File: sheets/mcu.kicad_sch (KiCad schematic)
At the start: 37 parts, among them SW1 SW_Nidec_CAS-120A1, SW2 SW_Push, U1 STM32H755ZIT6, Y1 25M, Y2 Crystal

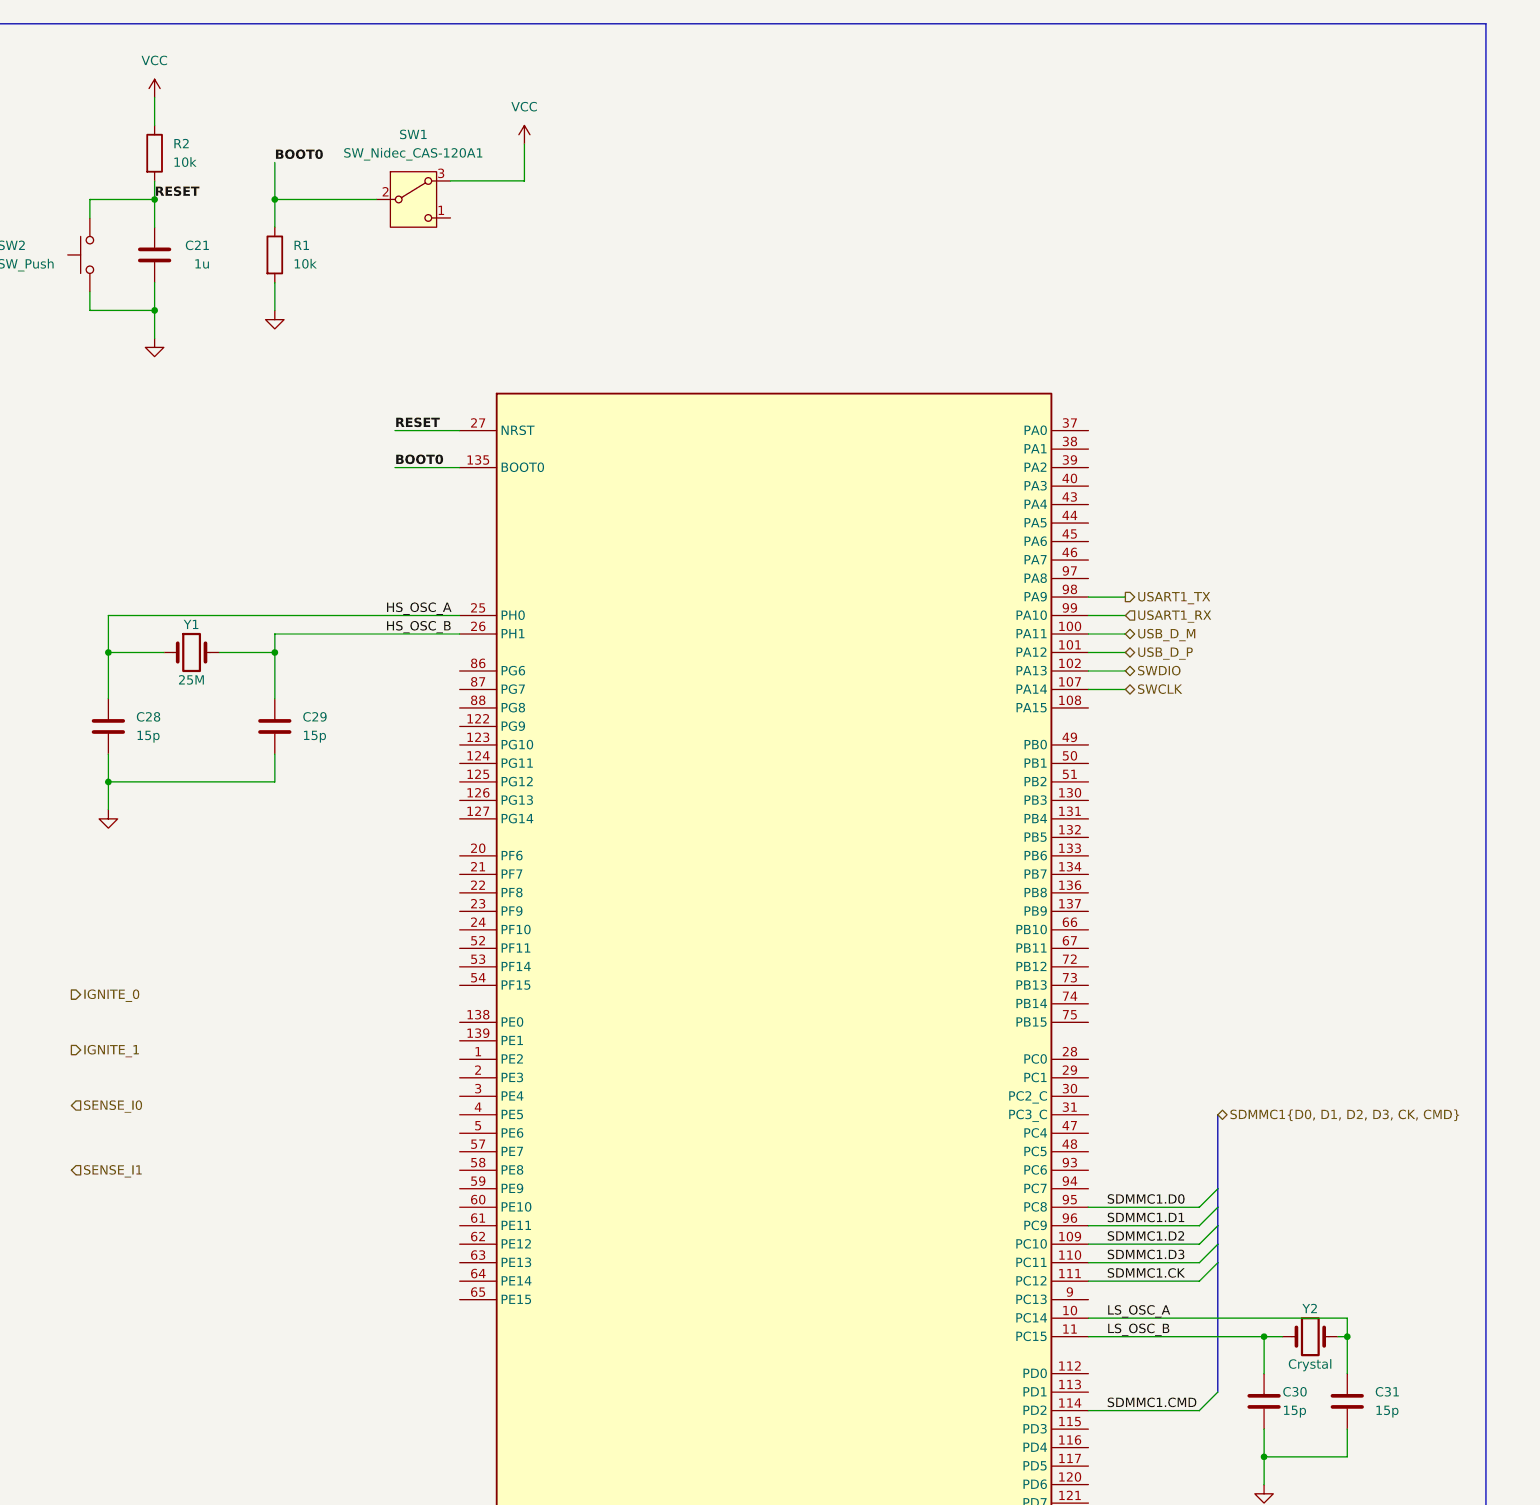
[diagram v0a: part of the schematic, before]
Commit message: added current rush limiting resistors to bmp581
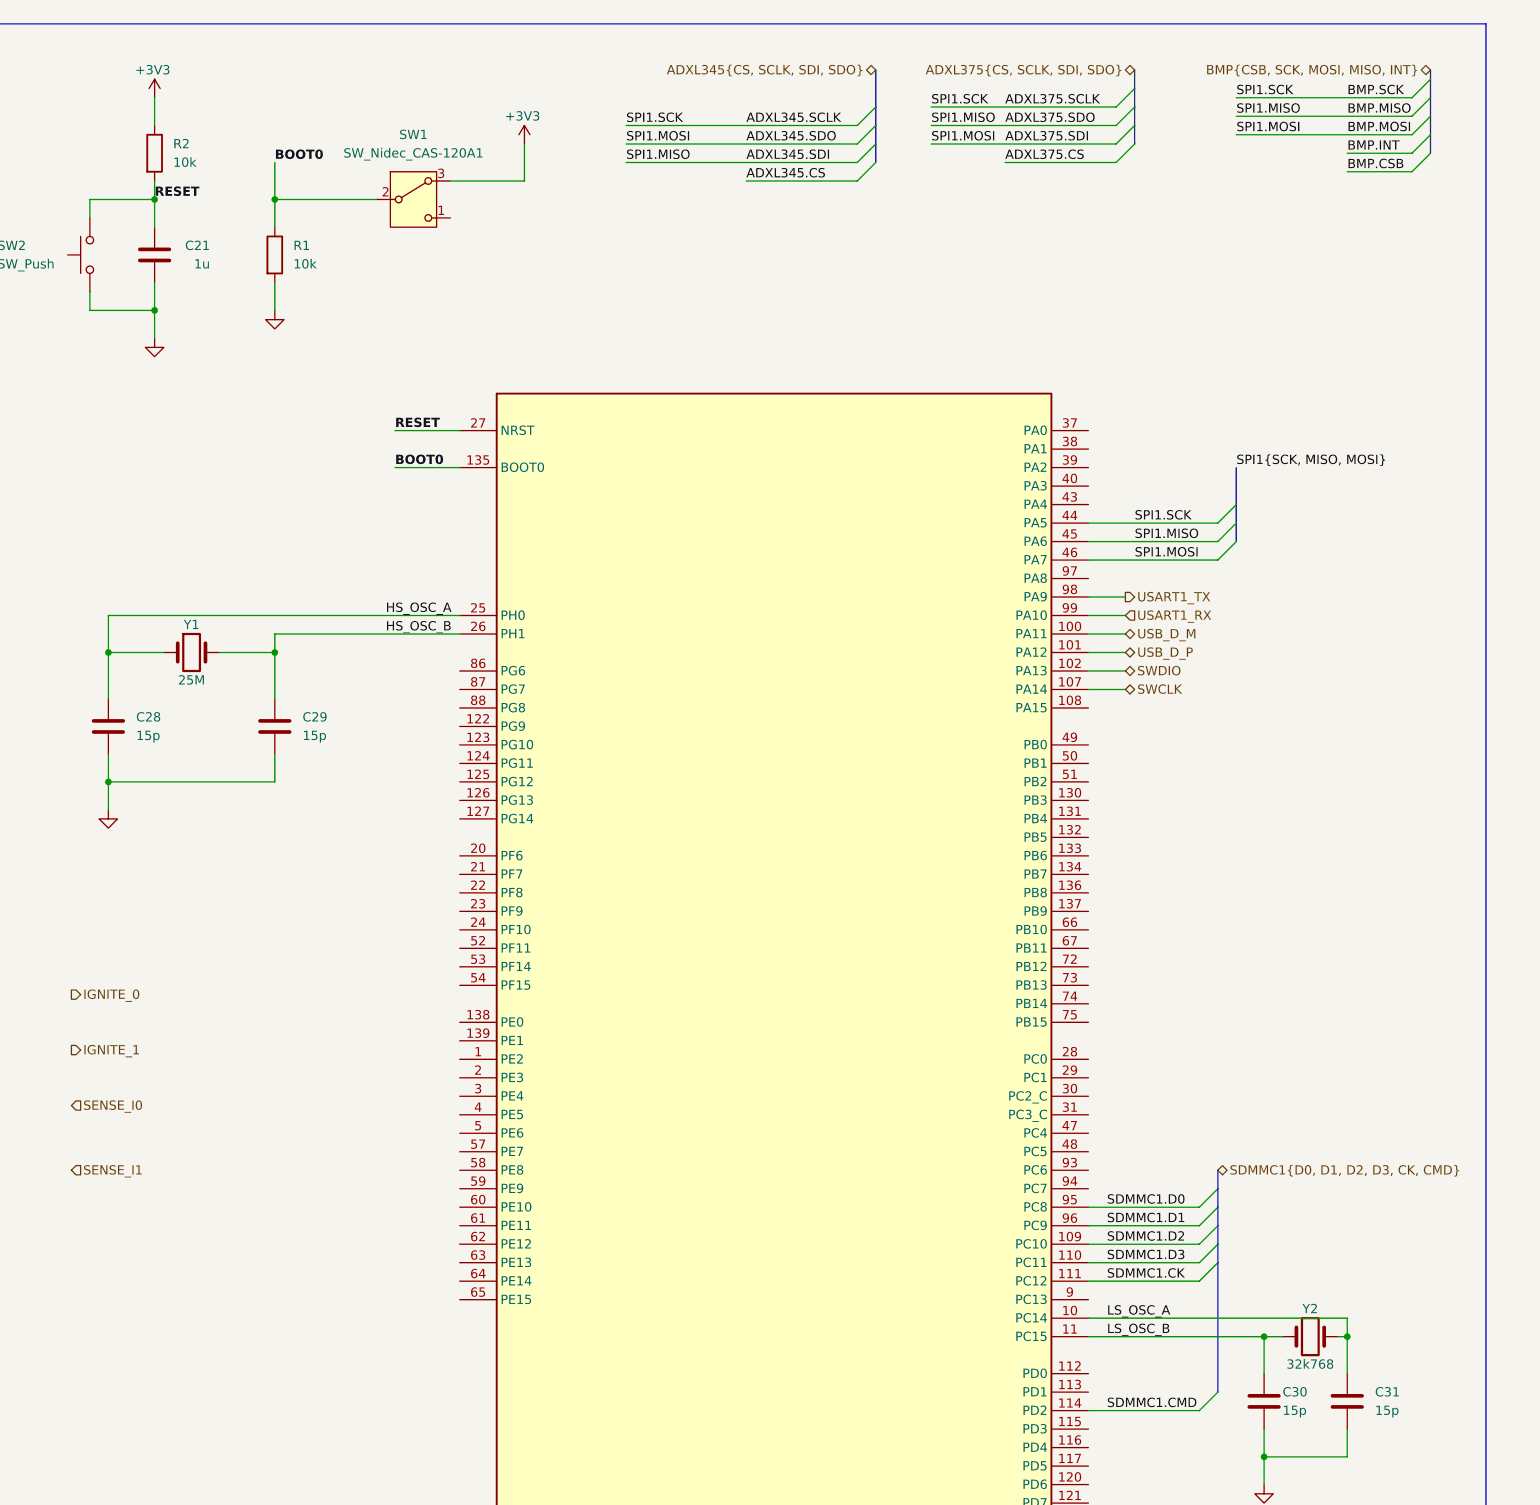
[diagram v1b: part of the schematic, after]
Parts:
- Y2: value Crystal -> 32k768
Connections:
- net VCC is gone; now on net +3V3: R2.1, SW1.3 (A)
- net ADXL345.SCLK: now reaches U1.44 (PA5)
- net ADXL345.SDI: now reaches U1.45 (PA6)
- net ADXL345.SDO: now reaches U1.46 (PA7)

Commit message: Added NEOM9N breakout symbol
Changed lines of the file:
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@@
+	)
+	(bus_entry
+		(at 322.58 36.83)
+		(size -2.54 2.54)
+		(stroke
+			(width 0)
+			(type default)
+		)
 	)
 	(bus_entry
@@
 		)
 	)
+	(bus_entry
+		(at 358.14 34.29)
+		(size -2.54 2.54)
+		(stroke
+			(width 0)
+			(type default)
+		)
+	)
 	(wire
 		(pts
@@
 		)
 	)
+	(bus
+		(pts
+			(xy 322.58 34.29) (xy 322.58 36.83)
+		)
+		(stroke
+			(width 0)
+			(type default)
+		)
+	)
 	(wire
 		(pts
@@
 		)
 	)
+	(bus
+		(pts
+			(xy 322.58 36.83) (xy 322.58 38.1)
+		)
+		(stroke
+			(width 0)
+			(type default)
+		)
+	)
 	(wire
 		(pts
@@
 	(wire
 		(pts
+			(xy 304.8 39.37) (xy 320.04 39.37)
+		)
+		(stroke
+			(width 0)
+			(type default)
+		)
+	)
+	(wire
+		(pts
 			(xy 119.38 82.55) (xy 121.92 82.55)
 		)
@@
 	(bus
 		(pts
+			(xy 358.14 31.75) (xy 358.14 34.29)
+		)
+		(stroke
+			(width 0)
+			(type default)
+		)
+	)
+	(bus
+		(pts
 			(xy 398.78 27.94) (xy 398.78 30.48)
 		)
@@
 		(pts
 			(xy 63.5 223.52) (xy 66.04 223.52)
+		)
+		(stroke
+			(width 0)
+			(type default)
+		)
+	)
+	(wire
+		(pts
+			(xy 340.36 36.83) (xy 355.6 36.83)
 		)
 		(stroke
@@
 		)
 	)
+	(label "ADXL375.INT"
+		(at 340.36 36.83 0)
+		(effects
+			(font
+				(size 1.27 1.27)
+			)
+			(justify left bottom)
+		)
+	)
 	(label "SDMMC1.D1"
 		(at 354.33 180.34 0)
@@
 				(thickness 0.254)
 				(bold yes)
+			)
+			(justify left bottom)
+		)
+	)
+	(label "ADXL345.INT"
+		(at 304.8 39.37 0)
+		(effects
+			(font
+				(size 1.27 1.27)
 			)
 			(justify left bottom)
@@
 		)
 	)
-	(hierarchical_label "ADXL345{CS, SCLK, SDI, SDO}"
+	(hierarchical_label "ADXL345{CS, SCLK, SDI, SDO, INT}"
 		(shape bidirectional)
 		(at 322.58 21.59 180)
@@
 		)
 	)
-	(hierarchical_label "ADXL375{CS, SCLK, SDI, SDO}"
+	(hierarchical_label "ADXL375{CS, SCLK, SDI, SDO, INT}"
 		(shape bidirectional)
 		(at 358.14 21.59 180)

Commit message: Fixed up power, added remaining to do
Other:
- moved on the sheet: C21, R1, R2, SW1, SW2

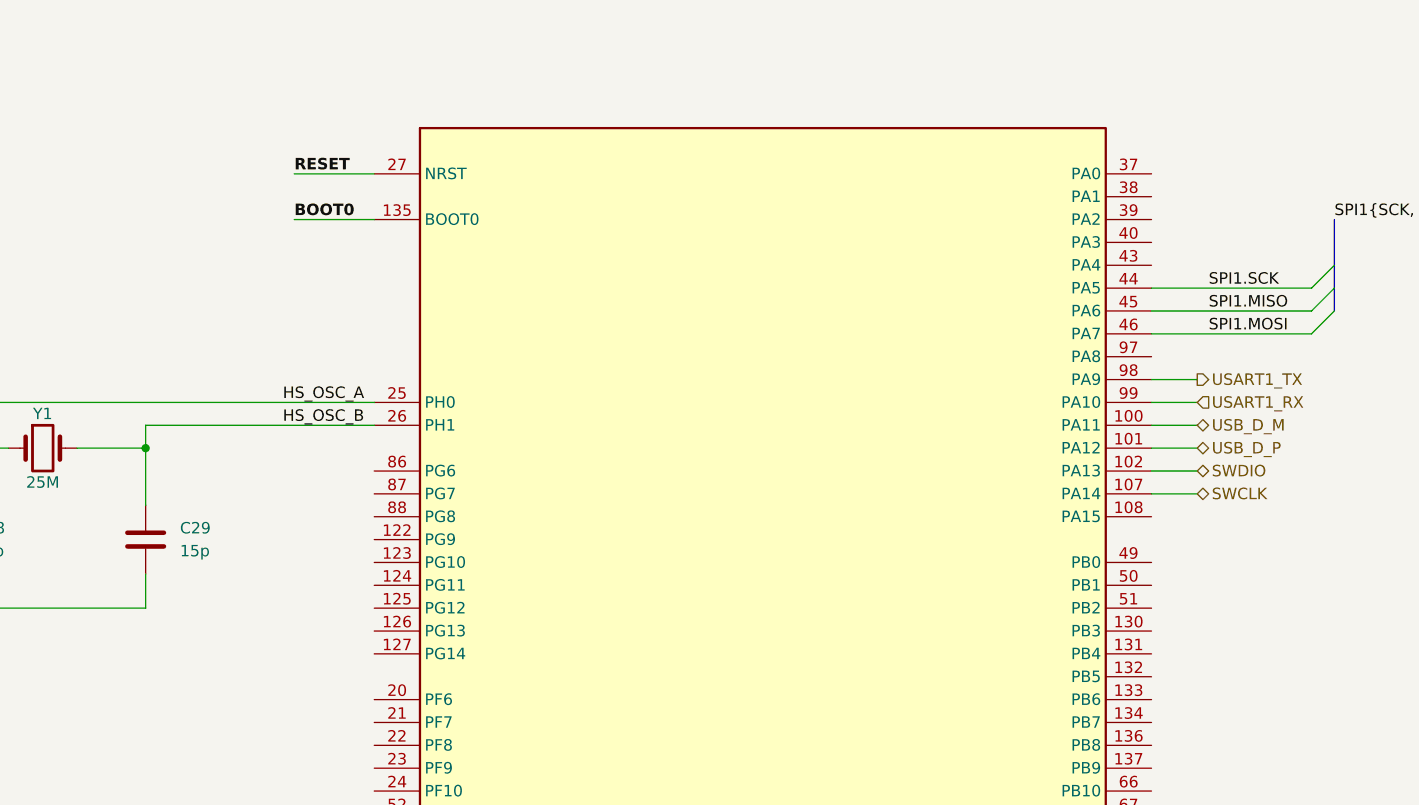
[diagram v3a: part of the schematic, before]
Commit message: polished up circuit, added new 16.8V to 7.4V step down circuit components
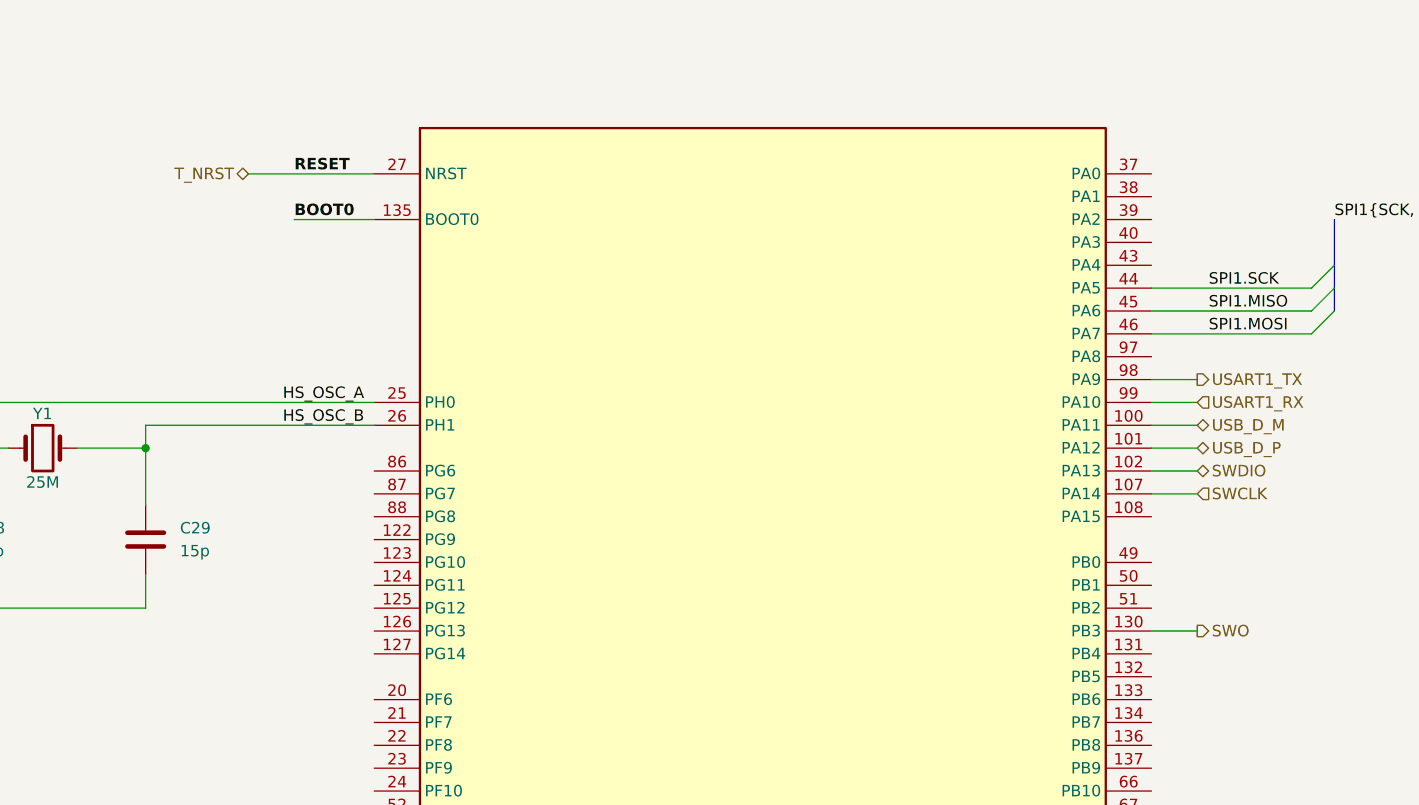
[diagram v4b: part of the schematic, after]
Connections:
- net SWO: now reaches U1.130 (PB3)
- net RESET renamed T_NRST
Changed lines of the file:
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@@
+		)
+	)
+	(wire
+		(pts
+			(xy 251.46 71.12) (xy 265.43 71.12)
+		)
+		(stroke
+			(width 0)
+			(type default)
 		)
 	)
@@
 	(wire
 		(pts
+			(xy 351.79 121.92) (xy 356.87 121.92)
+		)
+		(stroke
+			(width 0)
+			(type default)
+		)
+	)
+	(wire
+		(pts
 			(xy 124.46 57.15) (xy 139.7 57.15)
 		)
@@
 		(pts
 			(xy 34.29 106.68) (xy 34.29 107.95)
-		)
-		(stroke
-			(width 0)
-			(type default)
-		)
-	)
-	(wire
-		(pts
-			(xy 256.54 71.12) (xy 265.43 71.12)
 		)
 		(stroke
@@
 	)
 	(hierarchical_label "SWCLK"
-		(shape bidirectional)
+		(shape input)
 		(at 356.87 106.68 0)
 		(effects
@@
 		)
 	)
+	(hierarchical_label "SWO"
+		(shape output)
+		(at 356.87 121.92 0)
+		(effects
+			(font
+				(size 1.27 1.27)
+			)
+			(justify left)
+		)
+	)
 	(hierarchical_label "BMP{CSB, SCK, MOSI, MISO, INT}"
 		(shape bidirectional)
@@
 		)
 	)
+	(hierarchical_label "T_NRST"
+		(shape bidirectional)
+		(at 251.46 71.12 180)
+		(effects
+			(font
+				(size 1.27 1.27)
+			)
+			(justify right)
+		)
+	)

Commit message: second push
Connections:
- net USART2_TX: now reaches U1.39 (PA2)
- net USART2_RX: now reaches U1.40 (PA3)
- net NEOM9N_EXTI0: now reaches U1.49 (PB0)
- net NEOM9N_RST: now reaches U1.50 (PB1)
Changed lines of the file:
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@@
 	)
 	(bus_entry
-		(at 372.11 83.82)
+		(at 382.27 83.82)
 		(size -2.54 2.54)
 		(stroke
@@
 	)
 	(bus_entry
-		(at 372.11 86.36)
+		(at 382.27 86.36)
 		(size -2.54 2.54)
 		(stroke
@@
 	)
 	(bus_entry
-		(at 372.11 81.28)
+		(at 382.27 81.28)
 		(size -2.54 2.54)
 		(stroke
@@
 	(wire
 		(pts
-			(xy 351.79 121.92) (xy 356.87 121.92)
+			(xy 351.79 121.92) (xy 357.505 121.92)
 		)
 		(stroke
@@
 	(bus
 		(pts
-			(xy 372.11 83.82) (xy 372.11 86.36)
+			(xy 382.27 83.82) (xy 382.27 86.36)
 		)
 		(stroke
@@
 	(bus
 		(pts
-			(xy 372.11 81.28) (xy 372.11 83.82)
+			(xy 382.27 81.28) (xy 382.27 83.82)
 		)
 		(stroke
@@
 	(wire
 		(pts
+			(xy 351.79 76.2) (xy 356.87 76.2)
+		)
+		(stroke
+			(width 0)
+			(type default)
+		)
+	)
+	(wire
+		(pts
 			(xy 96.52 36.83) (xy 107.95 36.83)
 		)
@@
 	(wire
 		(pts
-			(xy 351.79 86.36) (xy 369.57 86.36)
+			(xy 351.79 86.36) (xy 379.73 86.36)
 		)
 		(stroke
@@
 	(wire
 		(pts
+			(xy 351.79 116.84) (xy 357.505 116.84)
+		)
+		(stroke
+			(width 0)
+			(type default)
+		)
+	)
+	(wire
+		(pts
 			(xy 63.5 72.39) (xy 63.5 73.66)
 		)
@@
 	(wire
 		(pts
+			(xy 357.505 114.3) (xy 351.79 114.3)
+		)
+		(stroke
+			(width 0)
+			(type default)
+		)
+	)
+	(wire
+		(pts
 			(xy 21.59 115.57) (xy 21.59 116.84)
 		)
@@
 	(wire
 		(pts
-			(xy 351.79 83.82) (xy 369.57 83.82)
+			(xy 351.79 83.82) (xy 379.73 83.82)
 		)
 		(stroke
@@
 	(wire
 		(pts
-			(xy 351.79 88.9) (xy 369.57 88.9)
+			(xy 351.79 88.9) (xy 379.73 88.9)
 		)
 		(stroke
@@
 	(wire
 		(pts
+			(xy 351.79 78.74) (xy 356.87 78.74)
+		)
+		(stroke
+			(width 0)
+			(type default)
+		)
+	)
+	(wire
+		(pts
 			(xy 107.95 36.83) (xy 119.38 36.83)
 		)
@@
 	(bus
 		(pts
-			(xy 372.11 76.2) (xy 372.11 81.28)
+			(xy 382.27 76.2) (xy 382.27 81.28)
 		)
 		(stroke
@@
 	)
 	(label "SPI1.MISO"
-		(at 358.14 86.36 0)
+		(at 370.205 86.36 0)
 		(effects
 			(font
@@
 	)
 	(label "SPI1{SCK, MISO, MOSI}"
-		(at 372.11 76.2 0)
+		(at 382.27 76.2 0)
 		(effects
 			(font
@@
 	)
 	(label "SPI1.SCK"
-		(at 358.14 83.82 0)
+		(at 370.205 83.82 0)
 		(effects
 			(font
@@
 	)
 	(label "SPI1.MOSI"
-		(at 358.14 88.9 0)
+		(at 370.205 88.9 0)
 		(effects
 			(font
@@
 			)
 			(justify left bottom)
+		)
+	)
+	(hierarchical_label "NEOM9N_EXTI0"
+		(shape input)
+		(at 357.505 114.3 0)
+		(effects
+			(font
+				(size 1.27 1.27)
+			)
+			(justify left)
 		)
 	)
@@
 	(hierarchical_label "SWO"
 		(shape output)
-		(at 356.87 121.92 0)
+		(at 357.505 121.92 0)
 		(effects
 			(font
@@
 		)
 	)
+	(hierarchical_label "USART2_RX"
+		(shape input)
+		(at 356.87 78.74 0)
+		(effects
+			(font
+				(size 1.27 1.27)
+			)
+			(justify left)
+		)
+	)
 	(hierarchical_label "USART1_TX"
 		(shape output)
@@
 		)
 	)
+	(hierarchical_label "USART2_TX"
+		(shape output)
+		(at 356.87 76.2 0)
+		(effects
+			(font
+				(size 1.27 1.27)
+			)
+			(justify left)
+		)
+	)
 	(hierarchical_label "USB_D_M"
 		(shape bidirectional)
@@
 		(effects
 			(font
+				(size 1.27 1.27)
+			)
+			(justify left)
+		)
+	)
+	(hierarchical_label "NEOM9N_RST"
+		(shape output)
+		(at 357.505 116.84 0)
+		(effects
+			(font
